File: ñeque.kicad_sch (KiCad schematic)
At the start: 8 parts, among them IC1 MIC1555YM5-TR

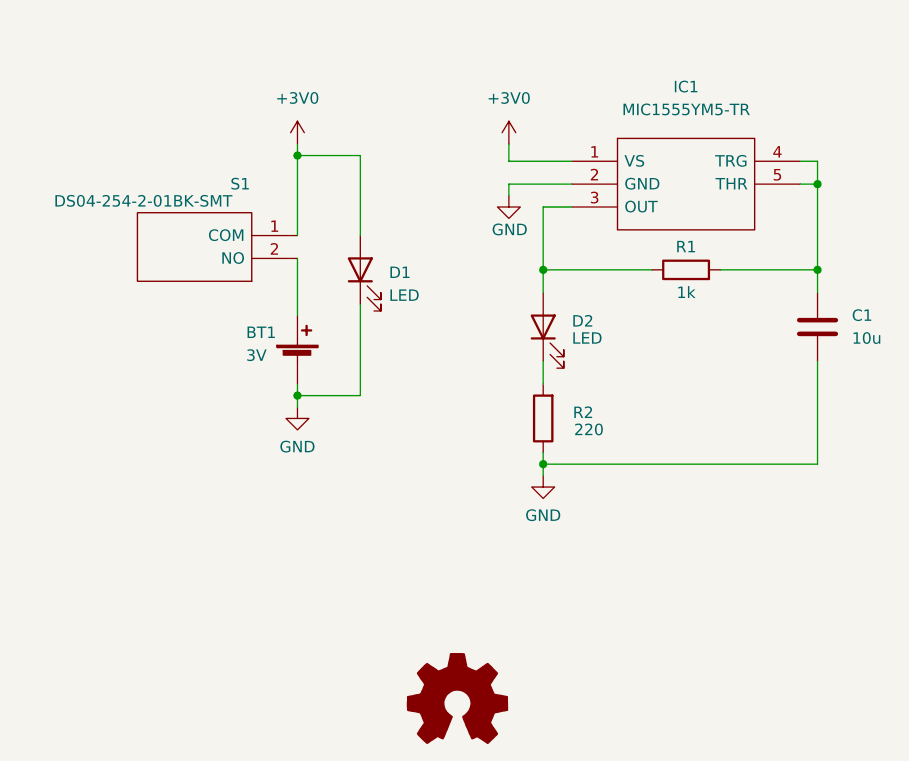
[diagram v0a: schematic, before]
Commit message: fixed resistor + LED
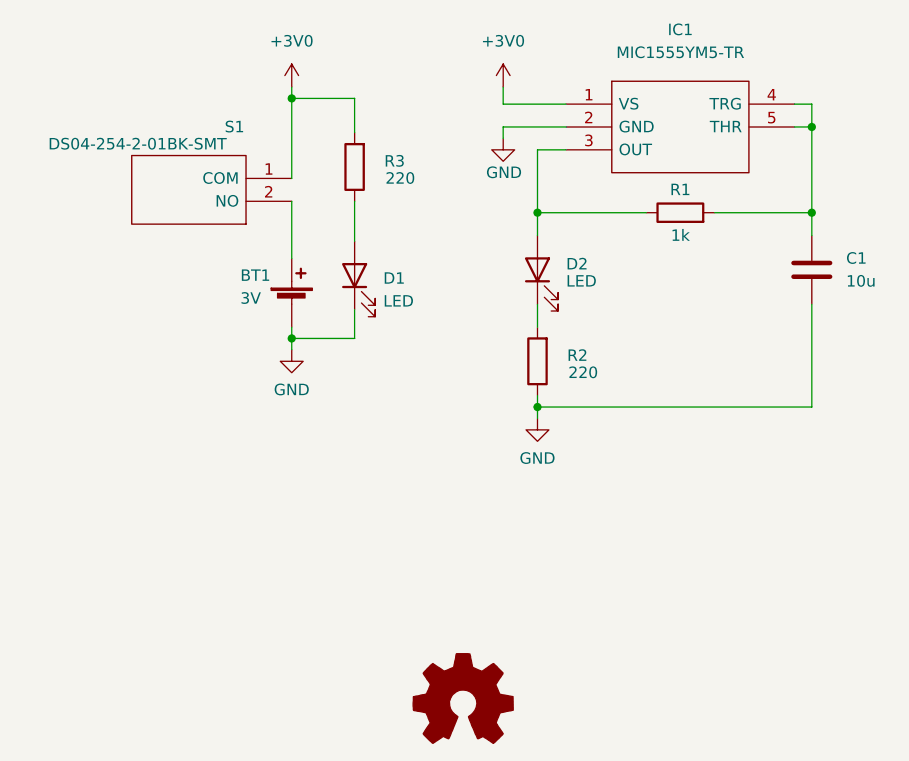
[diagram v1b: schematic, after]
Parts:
- added R3: 220, Resistor_SMD:R_0603_1608Metric, symbol Device:R
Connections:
- net +3V0: now also R3.2; no longer D1.2 (A)
- new net: D1.2 (A), R3.1
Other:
- moved on the sheet: BT1, C1, D1, D2, IC1, R1, R2, S1

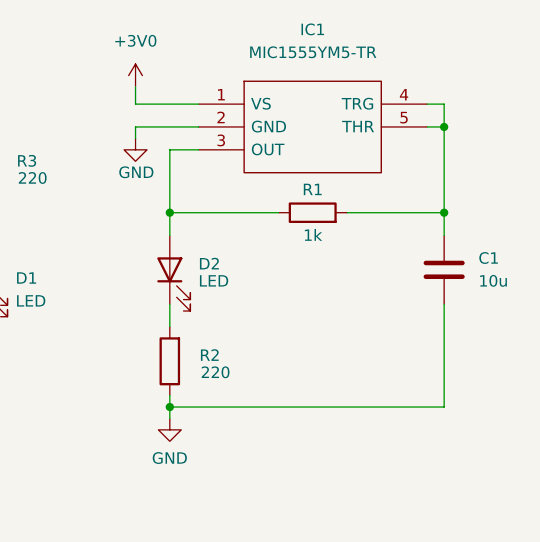
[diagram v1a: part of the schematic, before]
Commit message: updated RC values
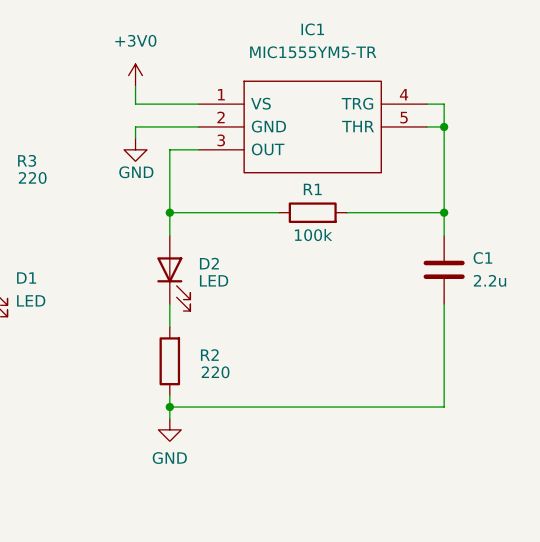
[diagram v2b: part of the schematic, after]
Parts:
- C1: value 10u -> 2.2u
- R1: value 1k -> 100k
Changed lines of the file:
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@@
   (symbol (lib_id "Device:C") (at 137.795 64.135 0) (unit 1)
     (in_bom yes) (on_board yes) (fields_autoplaced)
-    (property "Reference" "C1" (id 0) (at 141.605 62.8649 0)
-      (effects (font (size 1.27 1.27)) (justify left))
-    )
-    (property "Value" "10u" (id 1) (at 141.605 65.4049 0)
+    (property "Reference" "C1" (id 0) (at 140.97 62.8649 0)
+      (effects (font (size 1.27 1.27)) (justify left))
+    )
+    (property "Value" "2.2u" (id 1) (at 140.97 65.4049 0)
       (effects (font (size 1.27 1.27)) (justify left))
     )
@@
     (in_bom yes) (on_board yes)
     (property "Reference" "R1" (id 0) (at 123.19 55.245 90))
-    (property "Value" "1k" (id 1) (at 123.19 60.325 90))
+    (property "Value" "100k" (id 1) (at 123.19 60.325 90))
     (property "Footprint" "Resistor_SMD:R_0603_1608Metric" (id 2) (at 123.19 59.563 90)
       (effects (font (size 1.27 1.27)) hide)
@@
     )
     (path "/2ca6ef39-f815-4a9e-b02e-a2a5054b8953"
-      (reference "C1") (unit 1) (value "10u") (footprint "Capacitor_SMD:C_0603_1608Metric")
+      (reference "C1") (unit 1) (value "2.2u") (footprint "Capacitor_SMD:C_0603_1608Metric")
     )
     (path "/c28cf999-c472-4d6d-8841-418c1a00fcf3"
@@
     )
     (path "/9222debe-bc45-4771-8734-63571eeac135"
-      (reference "R1") (unit 1) (value "1k") (footprint "Resistor_SMD:R_0603_1608Metric")
+      (reference "R1") (unit 1) (value "100k") (footprint "Resistor_SMD:R_0603_1608Metric")
     )
     (path "/e9650f62-0b07-42b2-aac7-c30b4b10a148"
